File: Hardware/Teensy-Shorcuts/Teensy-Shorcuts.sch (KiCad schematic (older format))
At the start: 10 parts

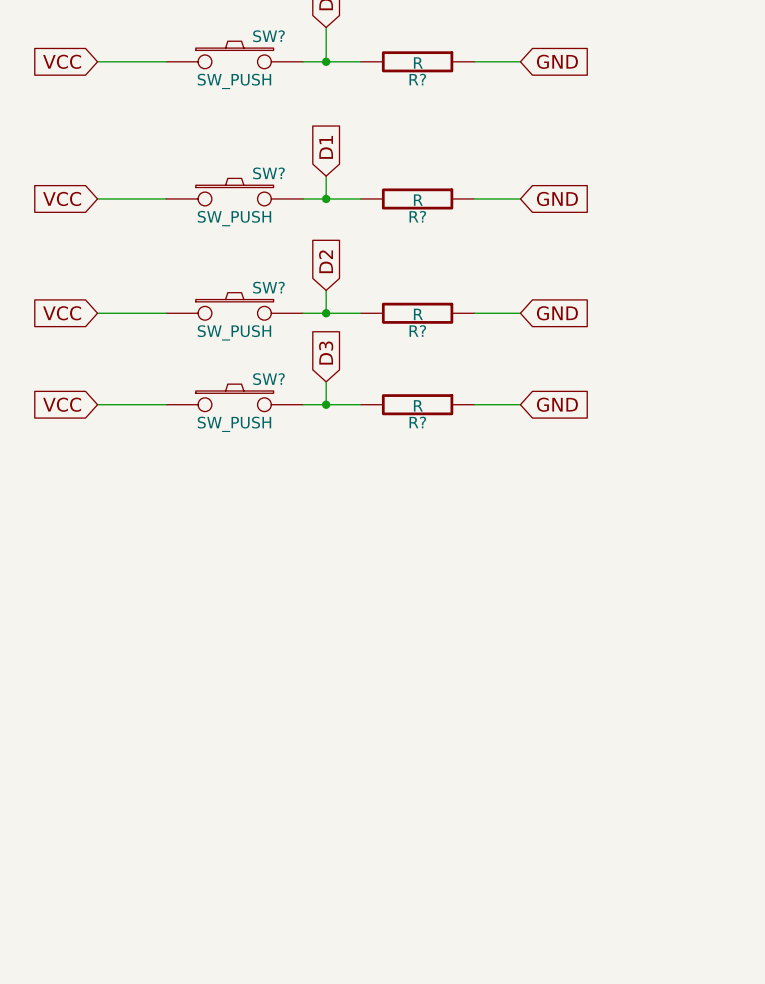
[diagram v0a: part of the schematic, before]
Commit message: added profile selector trimmer
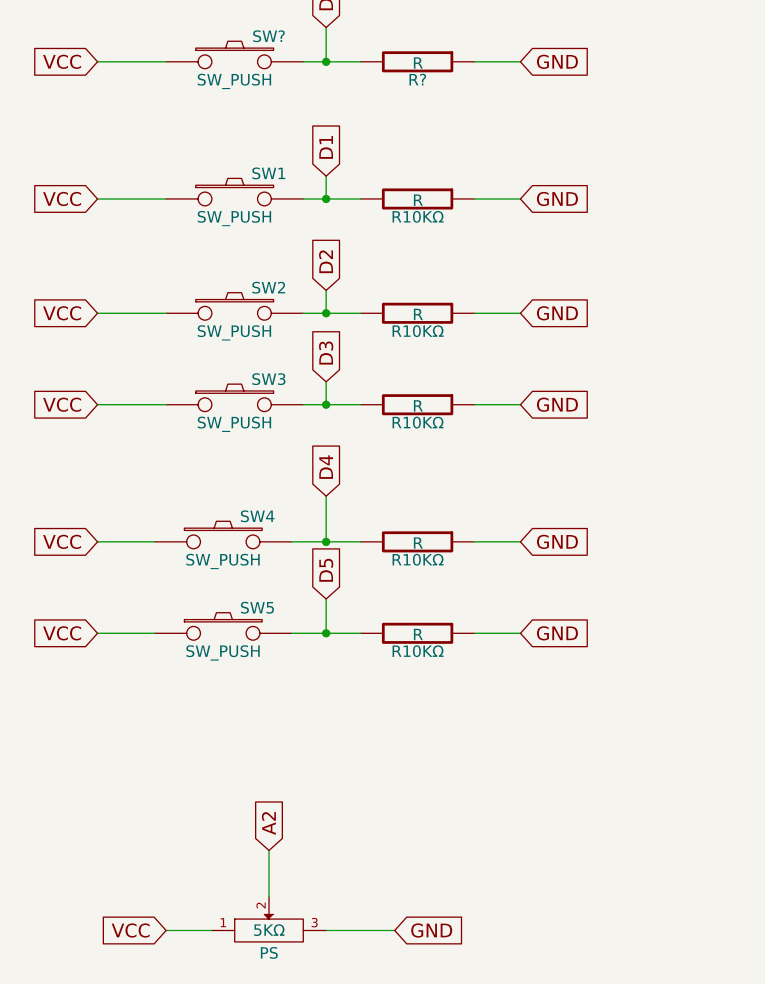
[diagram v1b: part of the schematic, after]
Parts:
- added PS: 5KΩ, symbol POT
- added R10KΩ (x2): R, symbol R
- added SW4, SW5: SW_PUSH, symbol SW_PUSH
- gave numbers to parts that had none: 4
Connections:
- net GND: now also PS.3, R10KΩ.1, R10KΩ.1
- net VCC: now also PS.1, SW4.1, SW5.1
- new net A2: PS.2
- new net D4: R10KΩ.2, SW4.2
- new net D5: R10KΩ.2, SW5.2
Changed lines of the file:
@@
 $EndComp
 $Comp
-L SW_PUSH SW?
+L SW_PUSH SW1
 U 1 1 55056234
 P 1850 1750
-F 0 "SW?" H 2000 1860 50  0000 C CNN
+F 0 "SW1" H 2000 1860 50  0000 C CNN
 F 1 "SW_PUSH" H 1850 1670 50  0000 C CNN
 F 2 "" H 1850 1750 60  0000 C CNN
@@
 $EndComp
 $Comp
-L SW_PUSH SW?
+L SW_PUSH SW2
 U 1 1 55056256
 P 1850 2250
-F 0 "SW?" H 2000 2360 50  0000 C CNN
+F 0 "SW2" H 2000 2360 50  0000 C CNN
 F 1 "SW_PUSH" H 1850 2170 50  0000 C CNN
 F 2 "" H 1850 2250 60  0000 C CNN
@@
 $EndComp
 $Comp
-L SW_PUSH SW?
+L SW_PUSH SW3
 U 1 1 55056277
 P 1850 2650
-F 0 "SW?" H 2000 2760 50  0000 C CNN
+F 0 "SW3" H 2000 2760 50  0000 C CNN
 F 1 "SW_PUSH" H 1850 2570 50  0000 C CNN
 F 2 "" H 1850 2650 60  0000 C CNN
@@
 $EndComp
 $Comp
-L R R?
+L R R10KΩ
 U 1 1 55056305
 P 2650 1750
-F 0 "R?" V 2730 1750 50  0000 C CNN
+F 0 "R10KΩ" V 2730 1750 50  0000 C CNN
 F 1 "R" V 2657 1751 50  0000 C CNN
 F 2 "" V 2580 1750 30  0000 C CNN
@@
 $EndComp
 $Comp
-L R R?
+L R R10KΩ
 U 1 1 5505632B
 P 2650 2250
-F 0 "R?" V 2730 2250 50  0000 C CNN
+F 0 "R10KΩ" V 2730 2250 50  0000 C CNN
 F 1 "R" V 2657 2251 50  0000 C CNN
 F 2 "" V 2580 2250 30  0000 C CNN
@@
 $EndComp
 $Comp
-L R R?
+L R R10KΩ
 U 1 1 55056352
 P 2650 2650
-F 0 "R?" V 2730 2650 50  0000 C CNN
+F 0 "R10KΩ" V 2730 2650 50  0000 C CNN
 F 1 "R" V 2657 2651 50  0000 C CNN
 F 2 "" V 2580 2650 30  0000 C CNN
@@
 Wire Wire Line
 	6100 2250 6100 1700
+Text GLabel 1250 3250 0    60   Input ~ 0
+VCC
+$Comp
+L SW_PUSH SW4
+U 1 1 550576AF
+P 1800 3250
+F 0 "SW4" H 1950 3360 50  0000 C CNN
+F 1 "SW_PUSH" H 1800 3170 50  0000 C CNN
+F 2 "" H 1800 3250 60  0000 C CNN
+F 3 "" H 1800 3250 60  0000 C CNN
+	1    1800 3250
+	1    0    0    -1
+$EndComp
+Text GLabel 2250 3050 1    60   Input ~ 0
+D4
+$Comp
+L R R10KΩ
+U 1 1 550576F6
+P 2650 3250
+F 0 "R10KΩ" V 2730 3250 50  0000 C CNN
+F 1 "R" V 2657 3251 50  0000 C CNN
+F 2 "" V 2580 3250 30  0000 C CNN
+F 3 "" H 2650 3250 30  0000 C CNN
+	1    2650 3250
+	0    1    1    0
+$EndComp
+Text GLabel 3100 3250 2    60   Input ~ 0
+GND
+Wire Wire Line
+	3100 3250 2900 3250
+Wire Wire Line
+	2100 3250 2400 3250
+Wire Wire Line
+	2250 3250 2250 3050
+Connection ~ 2250 3250
+Wire Wire Line
+	1500 3250 1250 3250
+Text GLabel 1250 3650 0    60   Input ~ 0
+VCC
+$Comp
+L SW_PUSH SW5
+U 1 1 55057826
+P 1800 3650
+F 0 "SW5" H 1950 3760 50  0000 C CNN
+F 1 "SW_PUSH" H 1800 3570 50  0000 C CNN
+F 2 "" H 1800 3650 60  0000 C CNN
+F 3 "" H 1800 3650 60  0000 C CNN
+	1    1800 3650
+	1    0    0    -1
+$EndComp
+$Comp
+L R R10KΩ
+U 1 1 550578E8
+P 2650 3650
+F 0 "R10KΩ" V 2730 3650 50  0000 C CNN
+F 1 "R" V 2657 3651 50  0000 C CNN
+F 2 "" V 2580 3650 30  0000 C CNN
+F 3 "" H 2650 3650 30  0000 C CNN
+	1    2650 3650
+	0    1    1    0
+$EndComp
+Text GLabel 3100 3650 2    60   Input ~ 0
+GND
+Wire Wire Line
+	2400 3650 2100 3650
+Wire Wire Line
+	1500 3650 1250 3650
+Wire Wire Line
+	3100 3650 2900 3650
+Text GLabel 2250 3500 1    60   Input ~ 0
+D5
+Wire Wire Line
+	2250 3500 2250 3650
+Connection ~ 2250 3650
+$Comp
+L POT PS
+U 1 1 55057DC3
+P 2000 4950
+F 0 "PS" H 2000 4850 50  0000 C CNN
+F 1 "5KΩ" H 2000 4950 50  0000 C CNN
+F 2 "" H 2000 4950 60  0000 C CNN
+F 3 "" H 2000 4950 60  0000 C CNN
+	1    2000 4950
+	1    0    0    -1
+$EndComp
+Text GLabel 1550 4950 0    60   Input ~ 0
+VCC
+Text GLabel 2550 4950 2    60   Input ~ 0
+GND
+Wire Wire Line
+	2550 4950 2250 4950
+Wire Wire Line
+	1750 4950 1550 4950
+Text GLabel 2000 4600 1    60   Input ~ 0
+A2
+Wire Wire Line
+	2000 4600 2000 4800
 $EndSCHEMATC

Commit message: added teensy 3.1/teensy 3.1 library created
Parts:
- added U?: Teensy_3.1, symbol Teensy_3.1
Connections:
- net 11: now also U?.11 (11(DOUT)); no longer DS?.11 (D4), DS?.12 (D5), DS?.13 (D6), DS?.14 (D7)
- net 12: now also U?.12 (12(DIN))
- net A2: now also U?.15 (15/A1)
- net D0: now also U?.0 (0(RX1))
- net D1: now also U?.1 (1(TX1))
- net D2: now also U?.2
- net D3: now also U?.3 (3(TX))
- net D4: now also U?.4 (4(RX))
- net D5: now also U?.5
- net GND: now also U?.27 (GND)
- new net 10: DS?.11 (D4), U?.10 (10(CS)(TX2))
- new net 7: DS?.14 (D7), U?.7 (7(RX3))
- new net 8: DS?.13 (D6), U?.8 (8(TX3))
- new net 9: DS?.12 (D5), U?.9 (9(RX2))
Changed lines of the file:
@@
 EESchema Schematic File Version 2
+LIBS:teensy_3.1
 LIBS:LCD20x4
 LIBS:power
@@
 	5200 1800 5200 1700
 Text GLabel 5700 1800 3    40   Input ~ 0
-11
+10
 Text GLabel 5800 1800 3    40   Input ~ 0
-11
+9
 Text GLabel 5900 1800 3    40   Input ~ 0
-11
+8
 Text GLabel 6000 1800 3    40   Input ~ 0
-11
+7
 Wire Wire Line
 	5700 1800 5700 1700
@@
 Wire Wire Line
 	2000 4600 2000 4800
+$Comp
+L Teensy_3.1 U?
+U 1 1 5506970B
+P 8250 4200
+F 0 "U?" H 8300 5250 60  0000 C CNN
+F 1 "Teensy_3.1" H 8350 5700 60  0000 C CNN
+F 2 "" H 8350 4200 60  0000 C CNN
+F 3 "" H 8350 4200 60  0000 C CNN
+	1    8250 4200
+	1    0    0    -1
+$EndComp
+Text GLabel 7050 4850 0    40   Input ~ 0
+12
+Text GLabel 7050 4700 0    40   Input ~ 0
+11
+Text GLabel 7050 4550 0    40   Input ~ 0
+10
+Text GLabel 7050 4400 0    40   Input ~ 0
+9
+Text GLabel 7050 4250 0    40   Input ~ 0
+8
+Text GLabel 7050 4100 0    40   Input ~ 0
+7
+Wire Wire Line
+	7050 4100 7250 4100
+Wire Wire Line
+	7250 4250 7050 4250
+Wire Wire Line
+	7050 4400 7250 4400
+Wire Wire Line
+	7250 4550 7050 4550
+Wire Wire Line
+	7250 4700 7050 4700
+Wire Wire Line
+	7250 4850 7050 4850
+Text GLabel 7050 3800 0    60   Input ~ 0
+D5
+Text GLabel 7050 3650 0    60   Input ~ 0
+D4
+Text GLabel 7050 3500 0    60   Input ~ 0
+D3
+Text GLabel 7050 3350 0    60   Input ~ 0
+D2
+Text GLabel 7050 3200 0    60   Input ~ 0
+D1
+Text GLabel 7050 3050 0    60   Input ~ 0
+D0
+Wire Wire Line
+	7250 3800 7050 3800
+Wire Wire Line
+	7050 3650 7250 3650
+Wire Wire Line
+	7250 3500 7050 3500
+Wire Wire Line
+	7050 3350 7250 3350
+Wire Wire Line
+	7250 3200 7050 3200
+Wire Wire Line
+	7050 3050 7250 3050
+Text GLabel 7050 2900 0    60   Input ~ 0
+GND
+Wire Wire Line
+	7050 2900 7250 2900
+Text GLabel 9450 4550 2    60   Input ~ 0
+A2
+Wire Wire Line
+	9450 4550 9250 4550
 $EndSCHEMATC

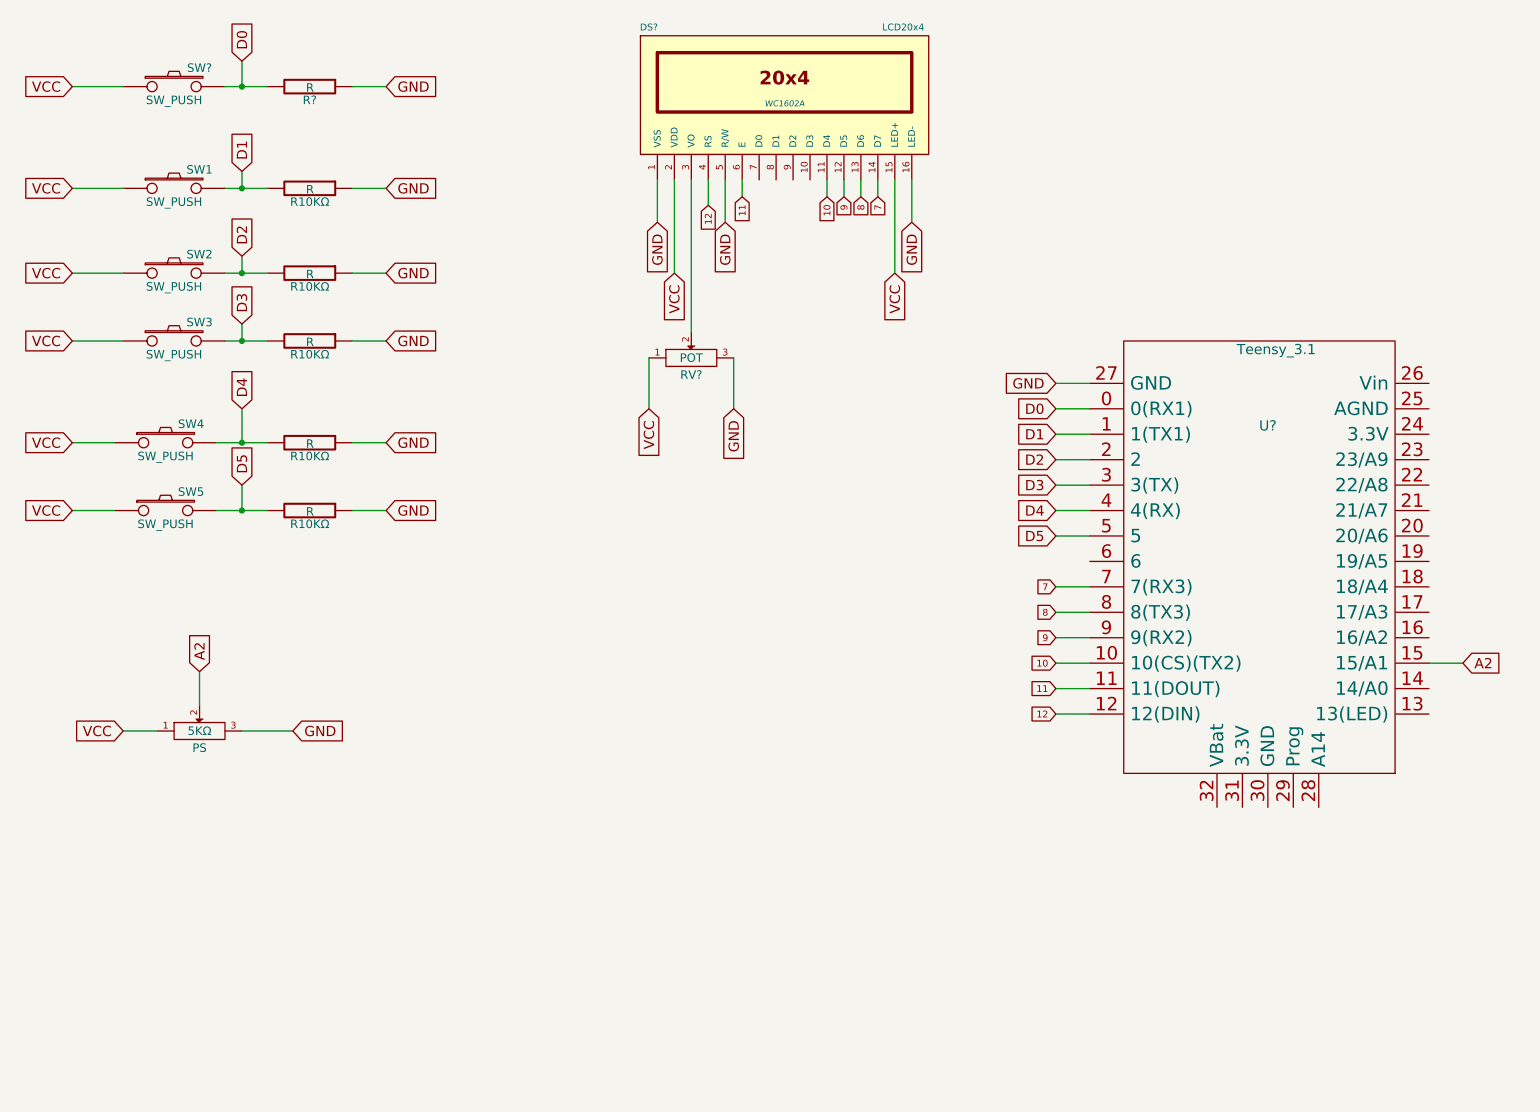
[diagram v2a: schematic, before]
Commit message: Created Schematichs and PCB board layaot
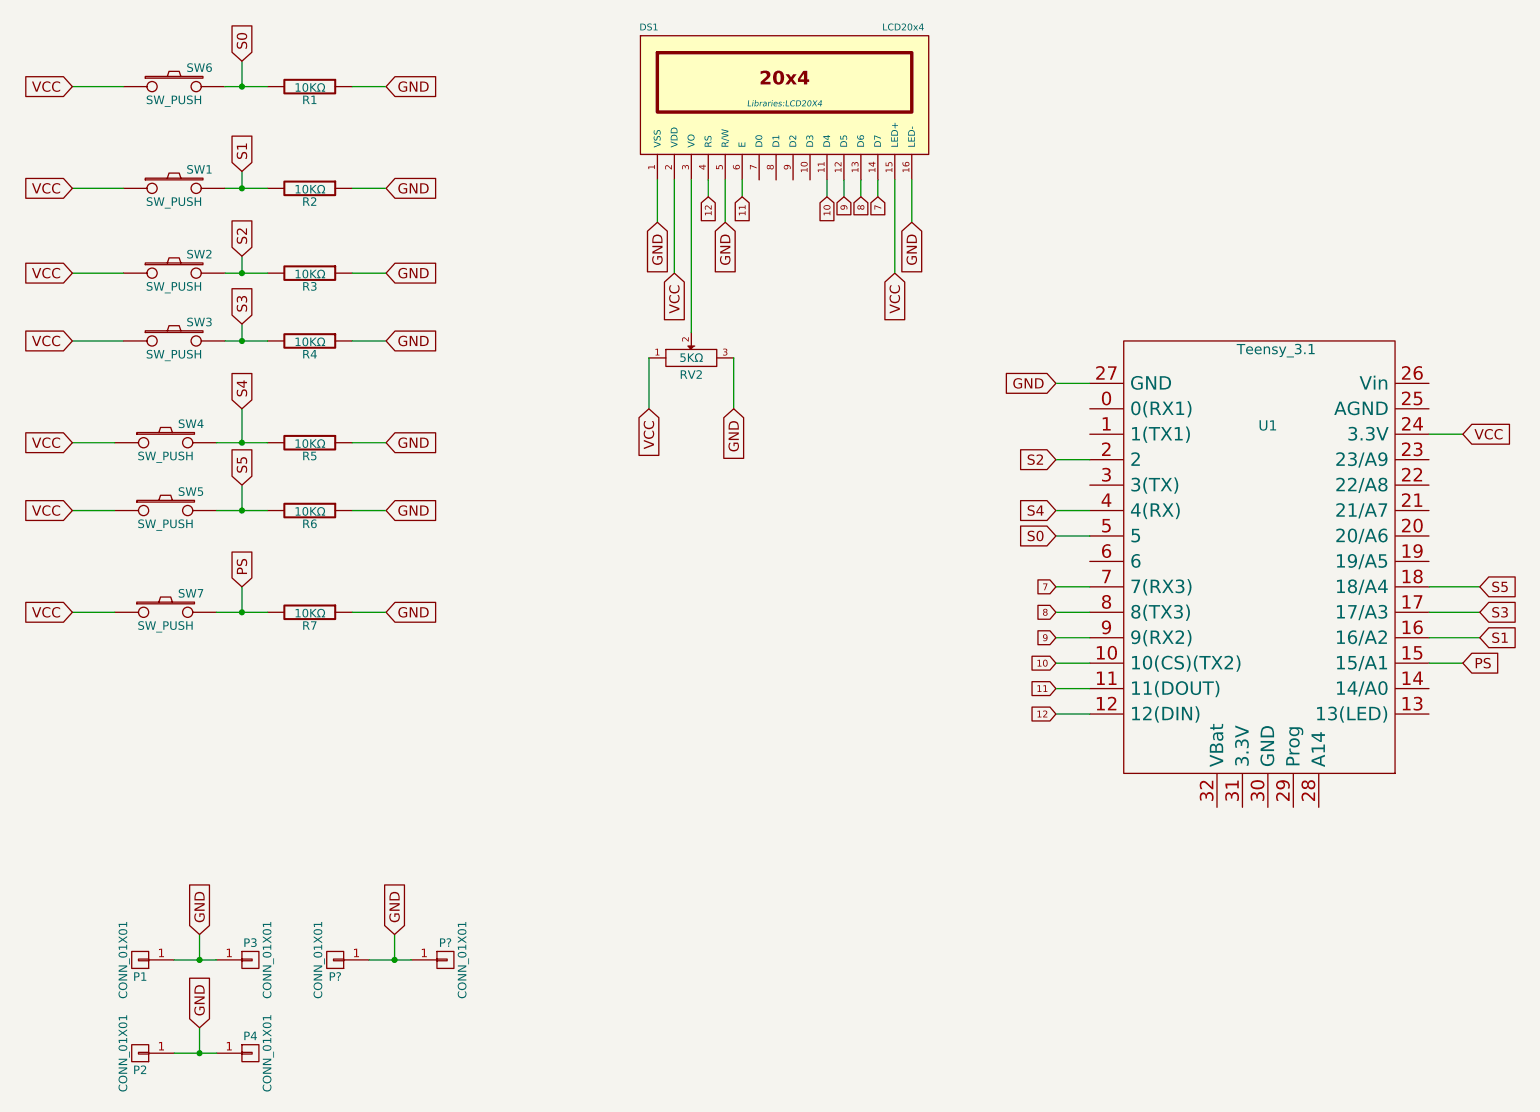
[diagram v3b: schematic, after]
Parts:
- removed PS: 5KΩ, symbol POT
- removed RV?: POT, symbol POT
- added P1, P2, P3, P4, P? (x2): CONN_01X01, Libraries:Jumper1x01, symbol CONN_01X01
- added R7: 10KΩ, Libraries:Res, symbol R
- added RV2: 5KΩ, Libraries:trimmer, symbol POT
- added SW7: SW_PUSH, Libraries:Switch, symbol SW_PUSH
- DS1: renamed from DS?; footprint WC1602A -> Libraries:LCD20X4
- R1: renamed from R?; value R -> 10KΩ; footprint (none) -> Libraries:Res
- R2, R3, R4, R5, R6: renamed from R10KΩ; value R -> 10KΩ; footprint (none) -> Libraries:Res
- SW1, SW2, SW3, SW4, SW5: footprint (none) -> Libraries:Switch
- SW6: renamed from SW?; footprint (none) -> Libraries:Switch
- U1: renamed from U?; footprint (none) -> Libraries:Teensy-3.1
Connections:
- net GND: now also P1.1 (P1), P2.1 (P1), P3.1 (P1), P4.1 (P1), P?.1 (P1), P?.1 (P1), R7.1, RV2.3
- net VCC: now also U1.24 (3.3V), RV2.1, SW7.1
- net at DS1.3 (VO): now also RV2.2
- net S1: now reaches U1.16 (16/A2)
- net S1: now also R2.2, SW1.2
- net S3: now reaches U1.17 (17/A3)
- net S3: now also R4.2, SW3.2
- net S5: now reaches U1.18 (18/A4)
- net S5: now also R6.2, SW5.2
- net A2 renamed PS
- net PS: now also R7.2, SW7.2
- net D0 renamed S0
- net S0: now also U1.5; no longer U1.0 (0(RX1))
- removed net D1: R2.2, SW1.2, U1.1 (1(TX1))
- net D2 renamed S2
- removed net D3: R4.2, SW3.2, U1.3 (3(TX))
- net D4 renamed S4
- removed net D5: R6.2, SW5.2, U1.5

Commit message: Modified pcb traces to delete 90º angles
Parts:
- gave numbers to parts that had none: 2
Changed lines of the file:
@@
 	9450 3200 9250 3200
 $Comp
-L CONN_01X01 P?
+L CONN_01X01 P6
 U 1 1 5507311C
 P 3450 6300
-F 0 "P?" H 3450 6400 50  0000 C CNN
+F 0 "P6" H 3450 6400 50  0000 C CNN
 F 1 "CONN_01X01" V 3550 6300 50  0000 C CNN
 F 2 "Libraries:Jumper1x01" H 3450 6300 60  0001 C CNN
@@
 $EndComp
 $Comp
-L CONN_01X01 P?
+L CONN_01X01 P5
 U 1 1 55073122
 P 2800 6300
-F 0 "P?" H 2800 6400 50  0000 C CNN
+F 0 "P5" H 2800 6400 50  0000 C CNN
 F 1 "CONN_01X01" V 2900 6300 50  0000 C CNN
 F 2 "Libraries:Jumper1x01" H 2800 6300 60  0001 C CNN
